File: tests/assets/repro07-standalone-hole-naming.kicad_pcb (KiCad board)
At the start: 2 copper layers, 20 x 20 mm, 2 parts

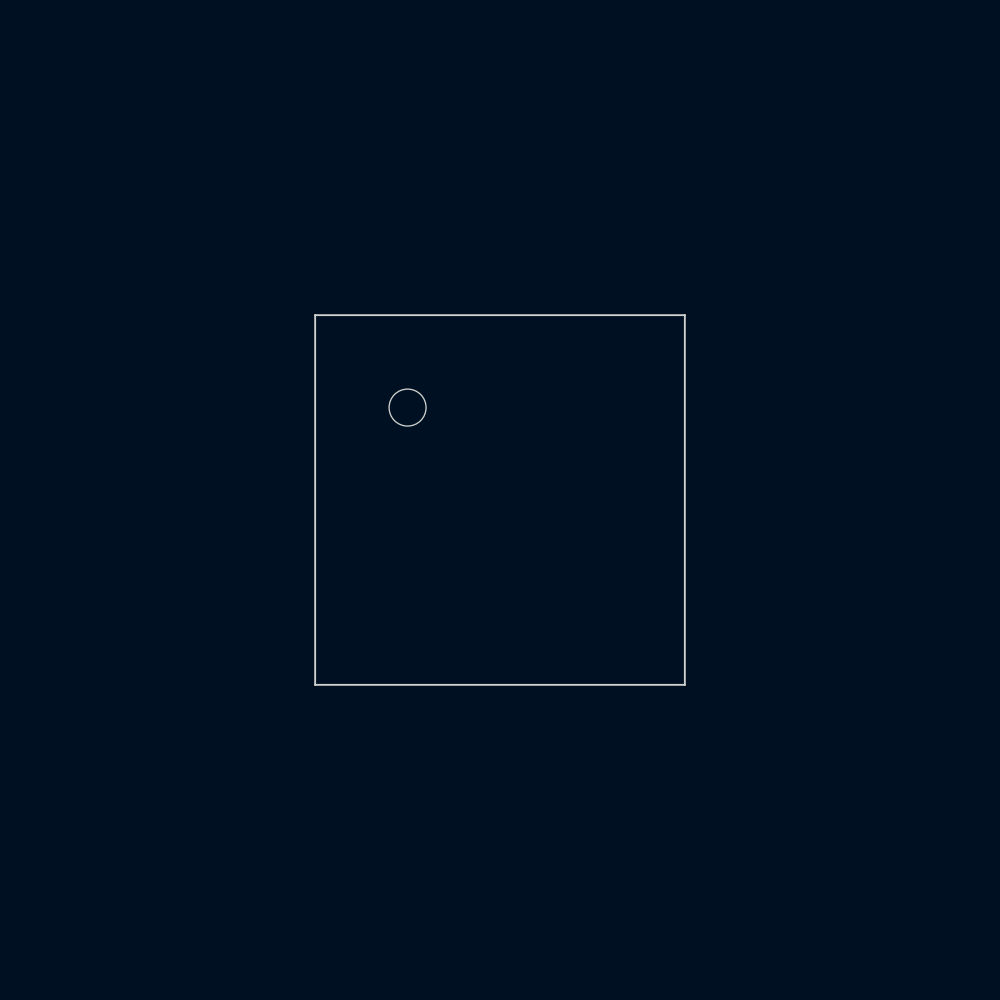
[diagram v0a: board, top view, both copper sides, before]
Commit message: feat: Dynamically footprints name for standalone PCB hole footprints in KiCad based on their shape and dimensions (#179)
* feat: Dynamically name standalone PCB hole footprints in KiCad based on their shape and dimensions

* update

* ne

* up

* up

* up test

* f
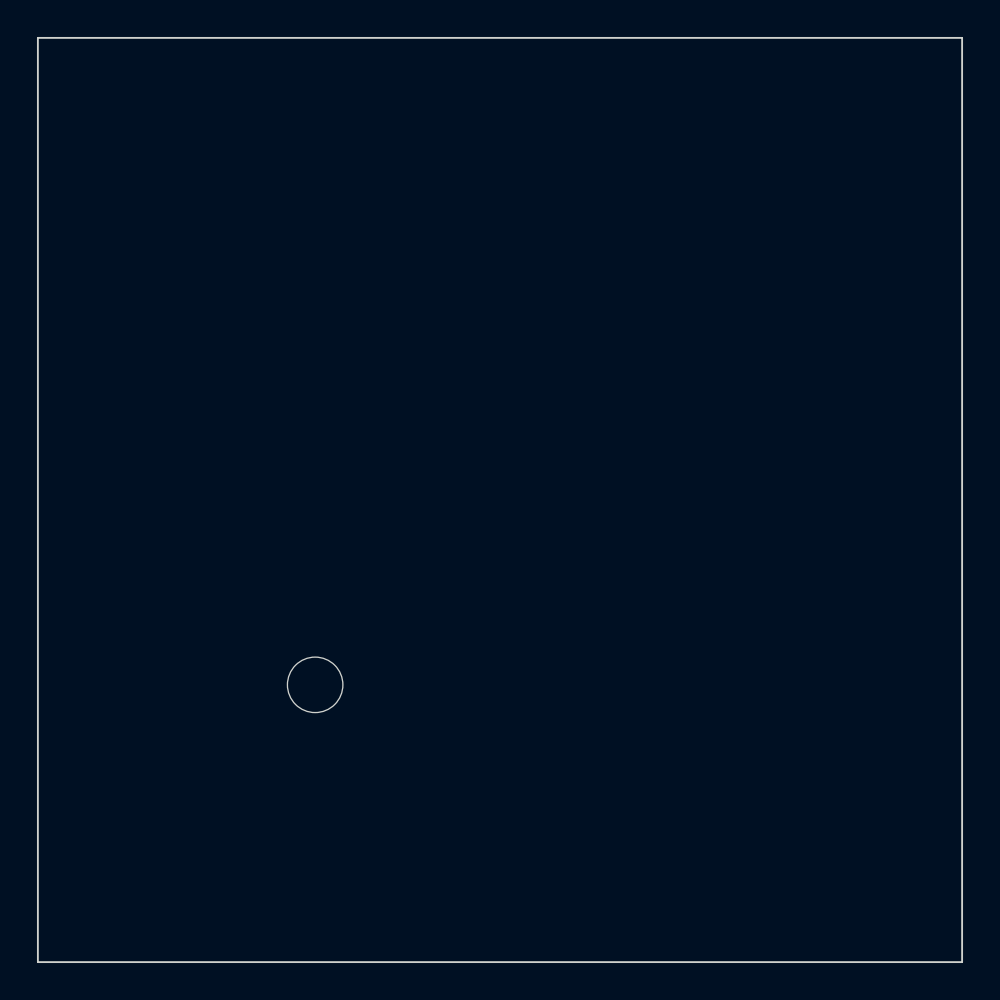
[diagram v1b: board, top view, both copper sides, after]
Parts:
- removed the ? at (100.0, 100.0) (x2)
- added ?: , tscircuit:hole_circle_holeDiameter3mm, F.Cu at (100.0, 100.0)
- added ?: , tscircuit:hole_pill_holeWidth4mm_holeHeight2mm, F.Cu at (100.0, 100.0)
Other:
- board size 20 x 20 mm -> 50 x 50 mm
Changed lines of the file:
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@@
   (net 0 "")
   (footprint
-    "tscircuit:hole_circle_holeDiameter2mm"
+    "tscircuit:hole_circle_holeDiameter3mm"
     (layer F.Cu)
     (at 100 100 0)
     (pad "" np_thru_hole circle
-      (at -5 -5 0)
-      (size 2 2)
-      (drill 2)
+      (at -10 10 0)
+      (size 3 3)
+      (drill 3)
       (layers *.Cu *.Mask)
     )
   )
   (footprint
-    "tscircuit:hole_pill_holeWidth2mm_holeHeight4mm"
+    "tscircuit:hole_pill_holeWidth4mm_holeHeight2mm"
     (layer F.Cu)
     (at 100 100 0)
     (pad "" np_thru_hole oval
-      (at 5 -5 0)
-      (size 2 4)
-      (drill oval 2 4)
+      (at 10 -10 0)
+      (size 4 2)
+      (drill oval 4 2)
       (layers *.Cu *.Mask)
     )
   )
   (gr_line
-    (start 90 110)
-    (end 110 110)
+    (start 75 125)
+    (end 125 125)
     (width 0.1)
     (layer Edge.Cuts)
   )
   (gr_line
-    (start 110 110)
-    (end 110 90)
+    (start 125 125)
+    (end 125 75)
     (width 0.1)
     (layer Edge.Cuts)
   )
   (gr_line
-    (start 110 90)
-    (end 90 90)
+    (start 125 75)
+    (end 75 75)
     (width 0.1)
     (layer Edge.Cuts)
   )
   (gr_line
-    (start 90 90)
-    (end 90 110)
+    (start 75 75)
+    (end 75 125)
     (width 0.1)
     (layer Edge.Cuts)

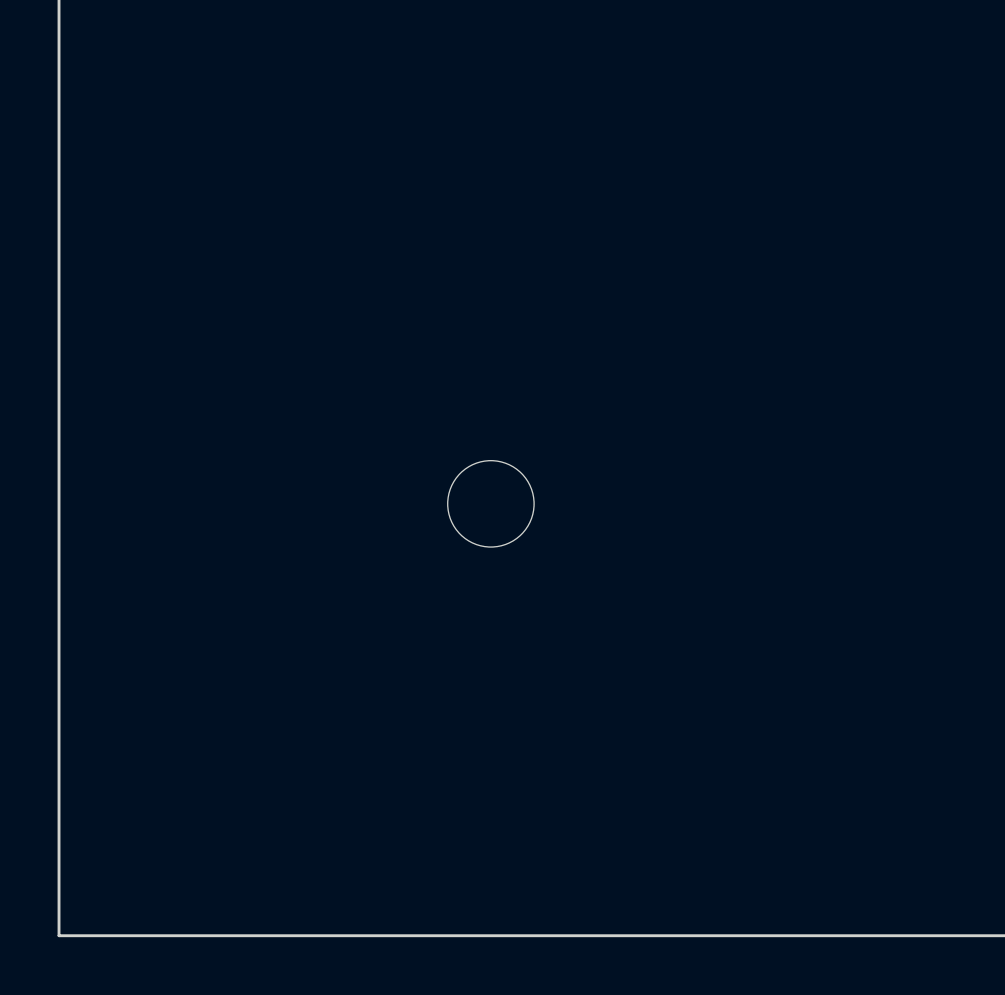
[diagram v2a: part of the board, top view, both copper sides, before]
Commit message: Support rotated_pill pcb_hole shapes in KiCad NPTH output (#195)
* Support rotated_pill pcb_hole shapes in KiCad NPTH output

* add test
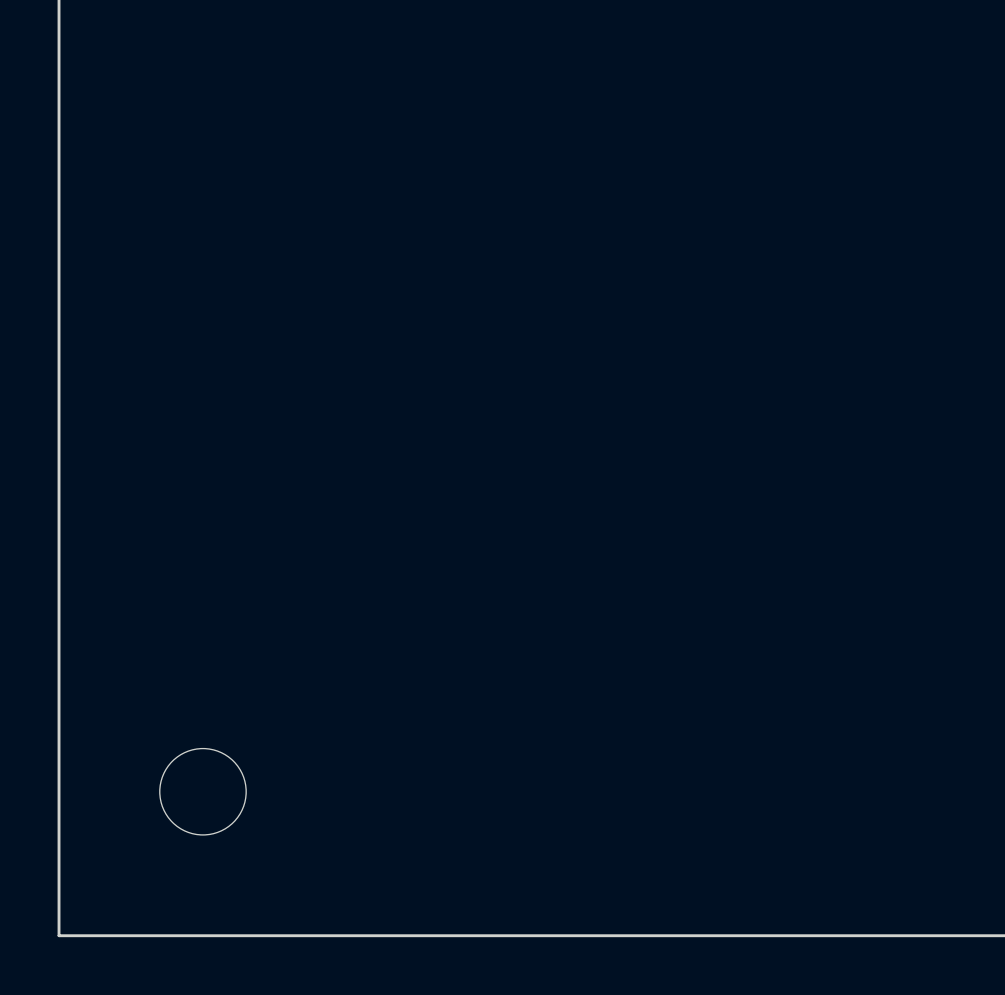
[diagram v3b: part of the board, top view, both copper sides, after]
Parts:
- added ?: , tscircuit:hole_rotated_pill_holeWidth4mm_holeHeight2mm_ccwRotation30deg, F.Cu at (100.0, 100.0)
- moved ? 14.1 mm to (90.0, 110.0)
- moved ? 14.1 mm to (110.0, 90.0)
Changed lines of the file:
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@@
     "tscircuit:hole_circle_holeDiameter3mm"
     (layer F.Cu)
-    (at 100 100 0)
+    (at 90 110 0)
     (pad "" np_thru_hole circle
       (at -10 10 0)
@@
     "tscircuit:hole_pill_holeWidth4mm_holeHeight2mm"
     (layer F.Cu)
+    (at 110 90 0)
+    (pad "" np_thru_hole oval
+      (at 0 0 0)
+      (size 4 2)
+      (drill oval 4 2)
+      (layers *.Cu *.Mask)
+    )
+  )
+  (footprint
+    "tscircuit:hole_rotated_pill_holeWidth4mm_holeHeight2mm_ccwRotation30deg"
+    (layer F.Cu)
     (at 100 100 0)
     (pad "" np_thru_hole oval
-      (at 10 -10 0)
+      (at 0 0 30)
       (size 4 2)
       (drill oval 4 2)
